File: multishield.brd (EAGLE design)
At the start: 49.7 x 53.2 mm, 1 part, among them J1 ARDUINO_R3_SHIELD

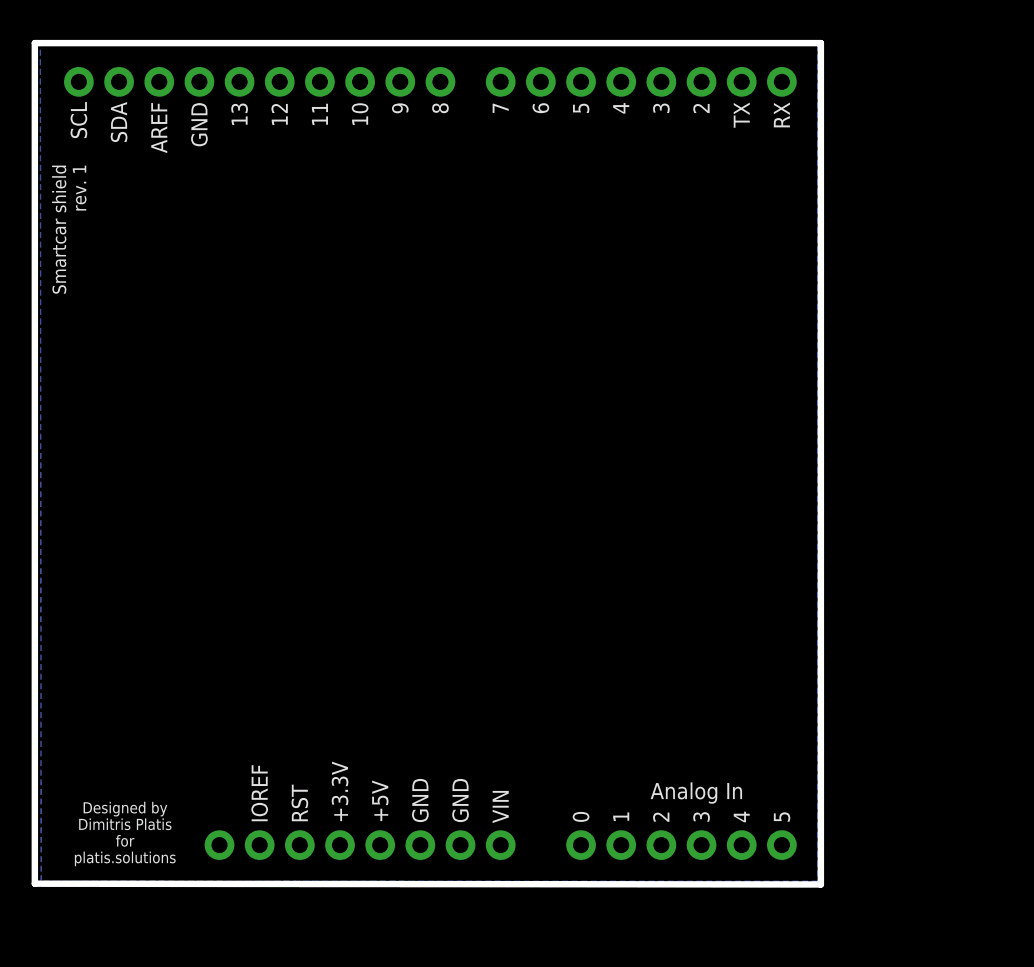
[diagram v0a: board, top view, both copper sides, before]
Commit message: adding shield with breakouts
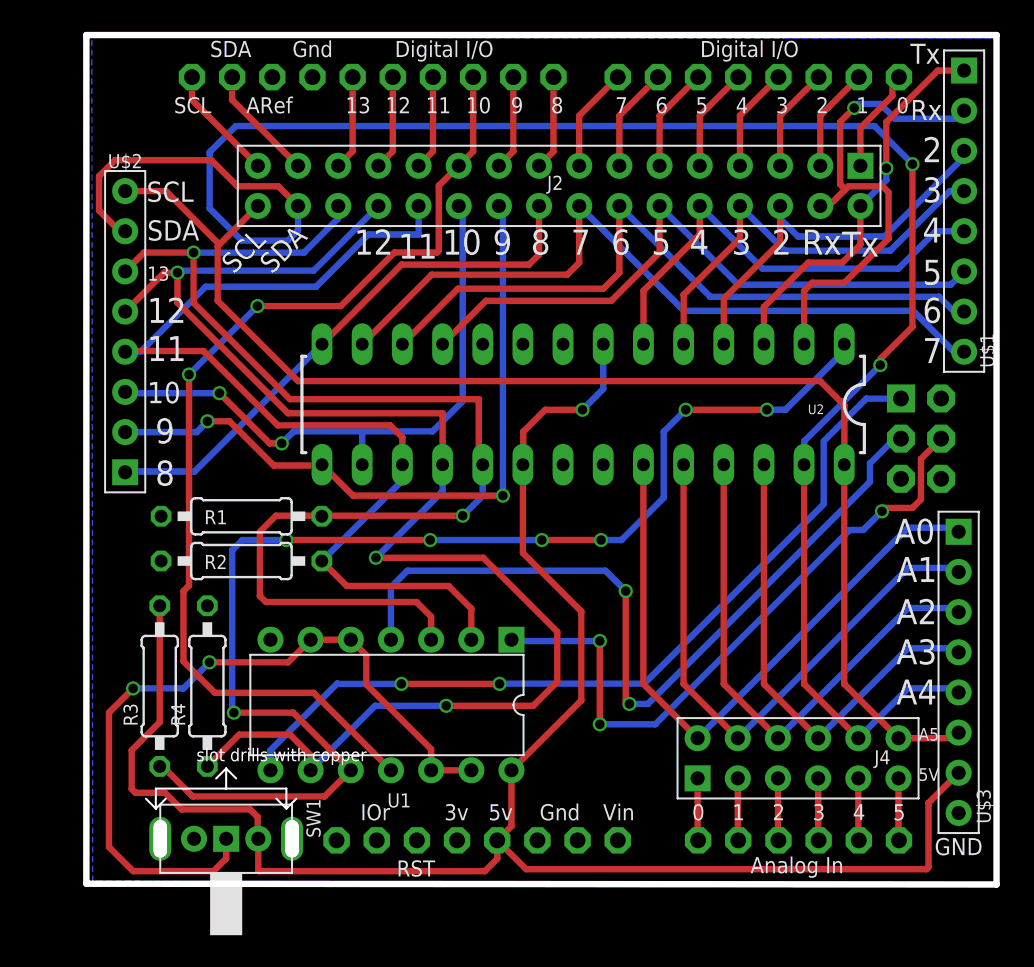
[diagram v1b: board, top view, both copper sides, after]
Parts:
- removed J1: ARDUINO_R3_SHIELD, SparkFun-Boards:UNO_R3_SHIELD
- added J2: 2x16p-2.54, Seeed-OPL-Connector:H2X16-2.54
- added J4: 2x6p-2.54, Seeed-OPL-Connector:H2X6-2.54
- added M1: ARDUINO_R3_ICSP, adafruit:ARDUINOR3_ICSP
- added R1, R2, R3, R4: 4.7K, Seeed-OPL-Resistor:PR-D2.3XL6.5MM
- added SW1: SK-12D01, Seeed-OPL-Button:SW5-2.0-8.8X4.4X4.7MM-90D
- added U$1, U$2, U$3: 8p-2.54, Seeed-OPL-Connector:H8-2.54
- added U1: AD595AQ-DIP14, Seeed-OPL-ic:DIP14-2.54-17.24X6.35MM
- added U2: ATMEGA328P_PDIP, SparkFun-DigitalIC:DIL28-3
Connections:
- new net 3V: M1.3V
- new net GND: M1.GND, M1.GND@1, M1.GND@2, M1.GND@3, R1.2, R2.2, R4.2, SW1.B, U$3.8, U1.7, U2.22, U2.8
- new net MISO: J2.20, R4.1, U$2.5, U1.9, U2.18
- new net MOSI: J2.21, R2.1, U$2.4, U1.2, U2.17
- new net N$11: J2.3, M1.D2
- new net N$12: J2.4, M1.D3
- new net N$13: J2.5, M1.D4
- new net N$14: J2.6, M1.D5
- new net N$15: J2.7, M1.D6
- new net N$16: J2.8, M1.D7
- new net N$17: J2.9, M1.D8
- new net N$18: J2.10, M1.D9
- new net N$19: J2.11, M1.D10, U1.11
- new net N$2: J2.1, M1.D0
- new net N$20: J2.12, M1.D11
- new net N$21: J2.13, M1.D12
- new net N$22: J2.14, M1.D13
- new net N$23: J2.15, M1.SDA
- new net N$24: J2.16, M1.SCL
- new net N$25: J2.32, U$1.1, U2.3
- new net N$26: J2.31, U$1.2, U2.2
- new net N$27: J2.30, U$1.3, U2.4
- new net N$28: J2.29, U$1.4, U2.5
- new net N$29: J2.28, U$1.5, U2.6
- new net N$30: J2.27, U$1.6, U2.11
- new net N$31: J4.1, M1.A0
- new net N$32: J2.25, U$1.8, U2.13
- new net N$33: J2.24, U$2.1, U2.14
- new net N$34: J2.23, U$2.2, U2.15
- new net N$35: J2.22, U$2.3, U2.16
- new net N$39: M1.MOSI, U1.1
- new net N$40: M1.SCK, U1.4
- new net N$41: J2.26, U$1.7, U2.12
- new net N$42: J4.2, M1.A1
- new net N$43: J4.3, M1.A2
- new net N$44: J4.4, M1.A3
- new net N$45: J4.12, U$3.1, U2.23
- new net N$46: J4.11, U$3.2, U2.24
- new net N$47: J4.10, U$3.3, U2.25
- new net N$48: J4.9, U$3.4, U2.26
- new net N$49: J2.18, J4.8, U$2.7, U$3.5, U2.27
- new net N$50: J2.17, J4.7, U$2.8, U$3.6, U2.28
- new net N$51: J4.5, M1.A4
- new net N$52: J4.6, M1.A5
- new net N$53: M1.MISO, U1.8
- new net N$56: SW1.COM, U1.12, U1.13, U1.5, U1.6
- new net N$9: J2.2, M1.D1
- new net SCK: J2.19, R1.1, U$2.6, U1.3, U2.19
- new net SLAVE-RESET: R3.1, U1.10, U2.1
- new net VCC: M1.5V, R3.2, SW1.A, U$3.7, U1.14, U2.20, U2.7
- new net VIN: M1.VIN
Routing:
- net N$49: track 0.00 -> 124.8 mm, vias 0 -> 2
- net VCC: track 0.00 -> 114.5 mm, vias 0 -> 1
- net MISO: track 0.00 -> 94.6 mm, vias 0 -> 3
- net N$50: track 0.00 -> 83.2 mm
- net SLAVE-RESET: track 0.00 -> 79.6 mm, vias 0 -> 7
- net SCK: track 0.00 -> 77.6 mm, vias 0 -> 2
- net MOSI: track 0.00 -> 65.8 mm
- net N$19: track 0.00 -> 65.2 mm, vias 0 -> 2
- net N$53: track 0.00 -> 52.7 mm, vias 0 -> 2
- net N$40: track 0.00 -> 51.2 mm, vias 0 -> 2
- net N$56: track 0.00 -> 48.2 mm, vias 0 -> 2
- net N$32: track 0.00 -> 47.6 mm
- net N$34: track 0.00 -> 44.6 mm, vias 0 -> 2
- net N$41: track 0.00 -> 44.4 mm
- net N$39: track 0.00 -> 41.5 mm, vias 0 -> 3
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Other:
- board size 49.7 x 53.2 mm -> 57.6 x 53.7 mm
- board text added: "10"
- board text added: "11"
- board text added: "12"
- board text added: "13"
- board text added: "2"
- board text added: "3"
- board text added: "4"
- board text added: "5"
- board text added: "5V"
- board text added: "6"
- board text added: "7"
- board text added: "8"
- board text added: "9"
- board text added: "A0"
- board text added: "A1"
- board text added: "A2"
- board text added: "A3"
- board text added: "A4"
- board text added: "A5"
- board text added: "GND"
- board text added: "Rx"
- board text added: "SCL"
- board text added: "SDA"
- board text added: "Tx"
- board text removed: "Designed by Dimitris Platis for platis.solutions"
- board text removed: "Smartcar shield rev. 1"

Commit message: added most of the things by now, minor aesthetic additions left for rev.0
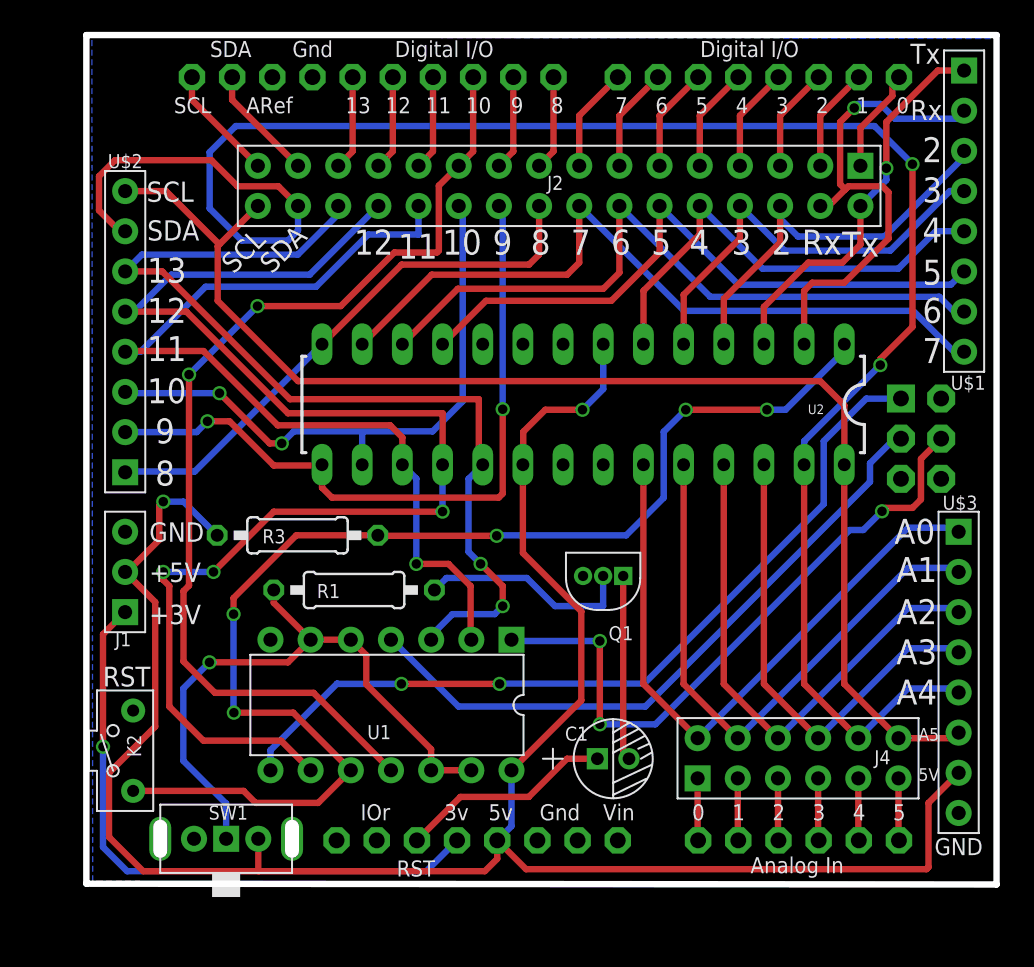
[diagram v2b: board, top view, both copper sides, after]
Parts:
- removed R2, R4: 4.7K, Seeed-OPL-Resistor:PR-D2.3XL6.5MM
- added C1: 100µF/16V 5X7, Seeed-OPL-Capacitor:PC-D5.0MM
- added J1: 3p-2.54, Seeed-OPL-Connector:H3-2.54
- added K2: TS-1101F, Seeed-OPL-Button:SW2-3.4X6.0X3.55MM-90D
- added Q1: BC547CZ1G, Seeed-OPL-Transistor:TO-92
- R1: value 4.7K -> 1K
- moved R3 13.1 mm to (16.2, 22.1), turned to 180 degrees
- moved R1 8.51 mm to (19.8, 18.7)
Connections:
- removed net 3V: M1.3V
- new net N$36: C1.-, Q1.1
- new net N$37: C1.+, M1.RESET
- new net N$38: Q1.2, R1.1
- new net N$54: J1.1, M1.3V
- net GND: now also J1.3, K2.P$2, Q1.3; no longer R1.2, R2.2, R4.2
- net MISO: no longer R4.1
- net MOSI: no longer R2.1
- net N$56: now also R1.2
- net SCK: no longer R1.1
- net SLAVE-RESET: now also K2.P$1
- net VCC: now also J1.2
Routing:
- net N$54: track 0.00 -> 39.3 mm, vias 0 -> 1
- net VCC: track 114.5 -> 131.0 mm, vias 1 -> 2
- net SCK: track 77.6 -> 61.2 mm
- net N$38: track 0.00 -> 13.6 mm
- net N$37: track 0.00 -> 13.5 mm
- net N$36: track 0.00 -> 11.7 mm
- net N$40: track 51.2 -> 41.7 mm, vias 2 -> 0
- net N$56: track 48.2 -> 39.5 mm, vias 2 -> 1
- net MISO: track 94.6 -> 86.2 mm
- net MOSI: track 65.8 -> 59.0 mm, vias 0 -> 1
- net N$34: track 44.6 -> 45.4 mm
- net SLAVE-RESET: track 79.6 -> 79.1 mm, vias 7 -> 5
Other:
- board text added: "+3V"
- board text added: "+5V"
- board text added: "RST"

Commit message: various improvements + clock
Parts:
- removed Q1: BC547CZ1G, Seeed-OPL-Transistor:TO-92
- added C2, C3: 22pf, Seeed-OPL-Capacitor:CERAMIC-2.54
- added Q2: (no value), SparkFun-DiscreteSemi:TO-92-AMMO
- added Y1: 16MHZ, Seeed-OPL-Crystal-Oscillator:HC49US
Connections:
- new net N$55: C2.2, U2.10, Y1.2
- new net N$57: C3.1, U2.9, Y1.1
- net GND: now also C2.1, C3.2, Q2.3; no longer Q1.3
- net N$36: now also Q2.1; no longer Q1.1
- net N$38: now also Q2.2; no longer Q1.2
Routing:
- net N$55: track 0.00 -> 38.8 mm, vias 0 -> 1
- net N$57: track 0.00 -> 30.4 mm, vias 0 -> 1
- net N$39: track 41.5 -> 50.2 mm
- net N$40: track 41.7 -> 47.3 mm, vias 0 -> 2
- net N$53: track 52.7 -> 58.2 mm
- net N$38: track 13.6 -> 9.78 mm
- net VCC: track 131.0 -> 133.3 mm
- net SCK: track 61.2 -> 60.1 mm
- net N$49: track 124.8 -> 125.9 mm
- net N$36: track 11.7 -> 12.4 mm
- net MISO: track 86.2 -> 85.6 mm
- net SLAVE-RESET: track 79.1 -> 79.7 mm, vias 5 -> 7
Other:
- board text added: "74HC4066-DIP14"
- board text added: "BC547"
- board text added: "Designed by Dimitris Platis for platis.solutions"
- board text added: "Moltoduino shield"
- board text added: "Moltoduino shield rev. 0"
- board text added: "designed by Dimitris Platis for platis.solutions"

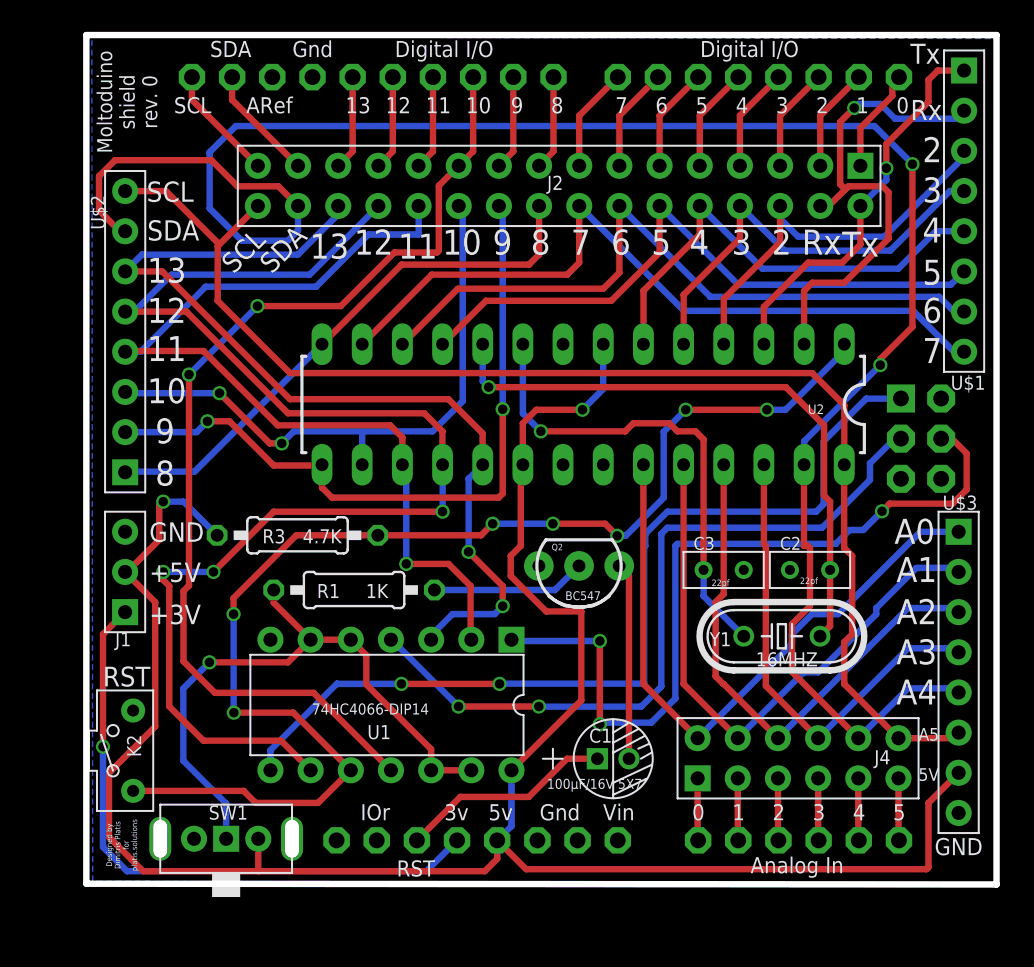
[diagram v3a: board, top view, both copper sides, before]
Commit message: part replacements and bom
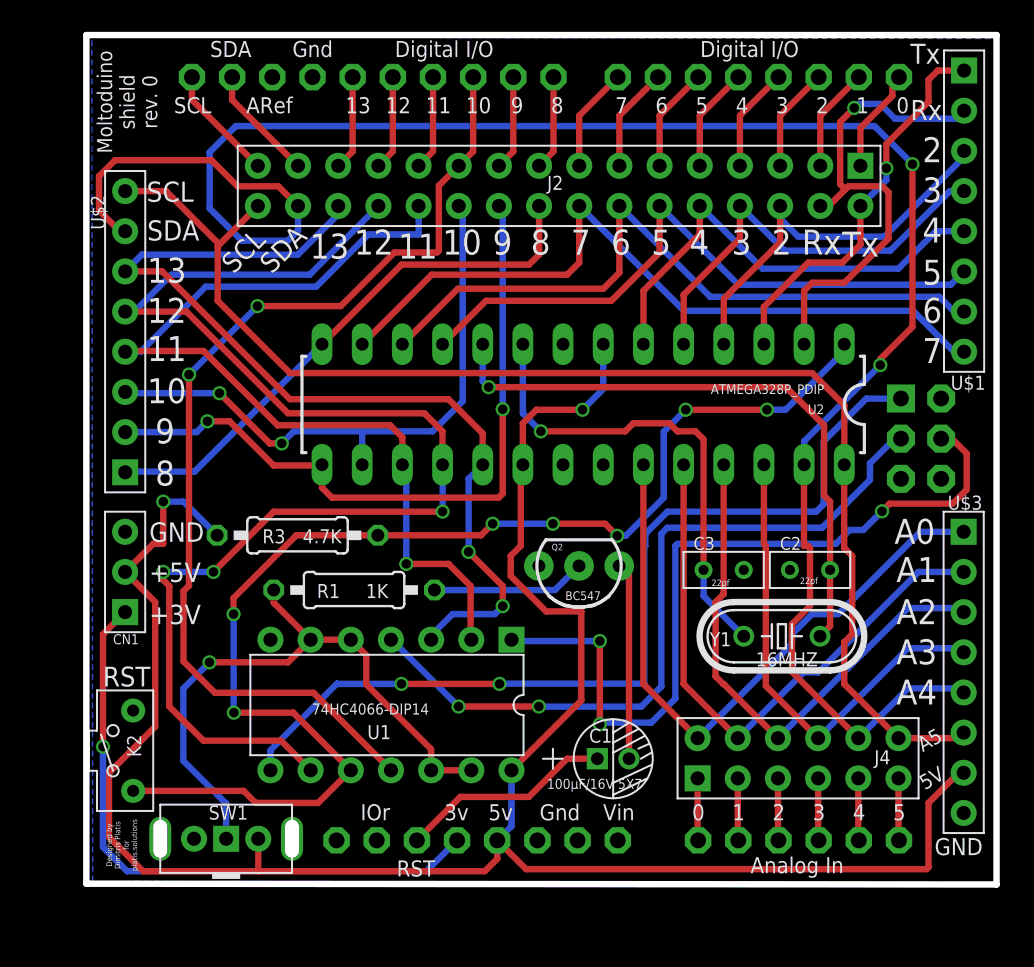
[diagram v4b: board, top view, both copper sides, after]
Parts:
- removed J1: 3p-2.54, Seeed-OPL-Connector:H3-2.54
- added CN1: 3P-2.54-90D, Seeed-OPL-Connector:H3-2.54-90D-FEMALE
- U$1, U$2, U$3: value 8p-2.54 -> 8p-2.54-90d; device Seeed-OPL-Connector:H8-2.54 -> Seeed-OPL-Connector:H8-2.54-90D-FEMALE
- moved U$3 0.32 mm to (58.2, 13.5)
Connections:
- net GND: now also CN1.3; no longer J1.3
- net N$54: now also CN1.1; no longer J1.1
- net VCC: now also CN1.2; no longer J1.2
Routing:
- net VCC: track 133.3 -> 133.9 mm
